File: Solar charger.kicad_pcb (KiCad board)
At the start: 2 copper layers, 70 x 32.5 mm, 12 parts, among them U1 MCP1700x-330xxTO

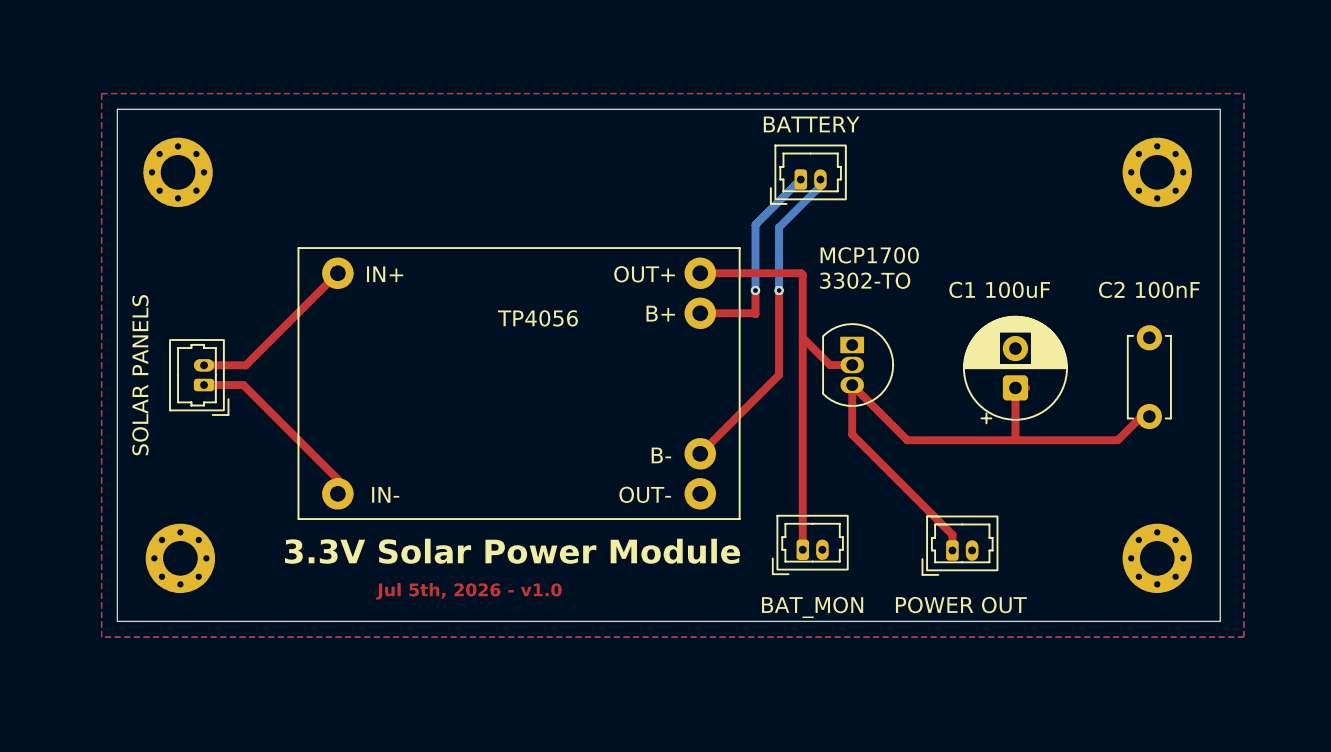
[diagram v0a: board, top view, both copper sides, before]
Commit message: Replace micro JSTs with terminal blocks (#3)
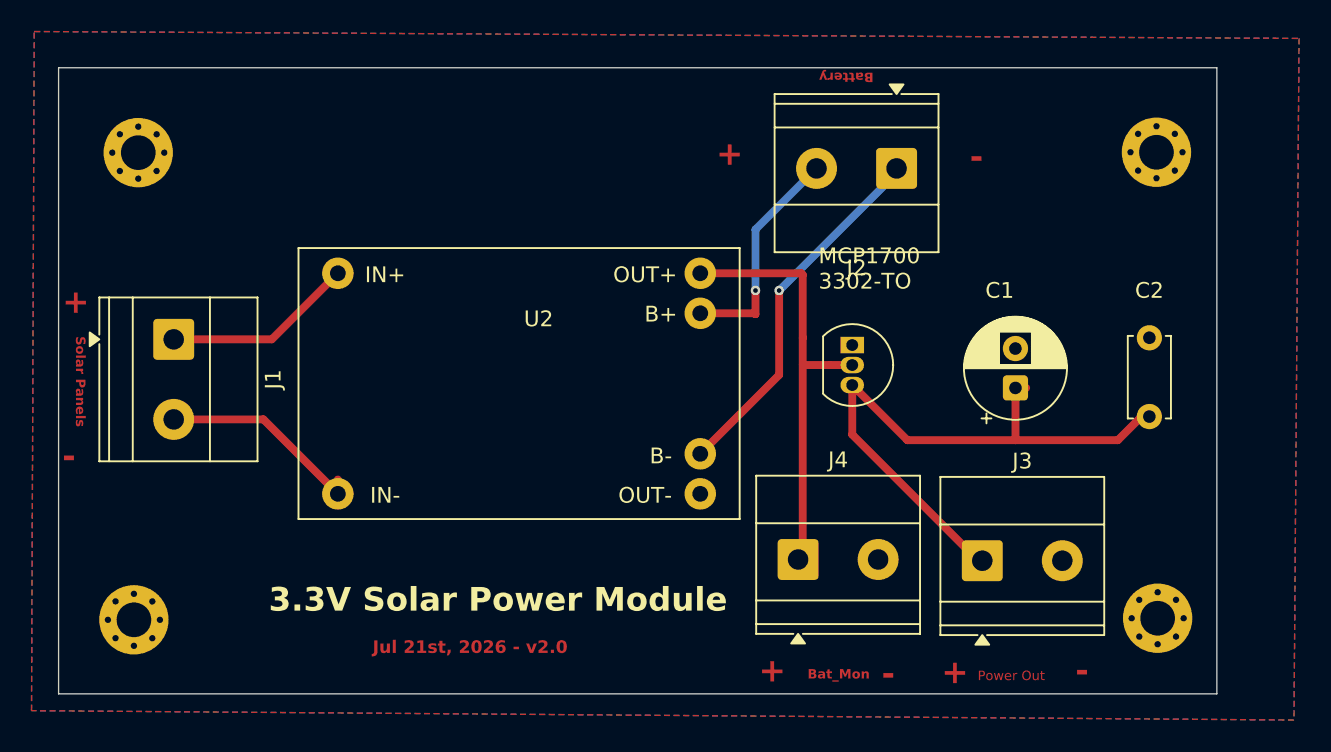
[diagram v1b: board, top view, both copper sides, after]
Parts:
- removed BATTERY: BATTERY, Connector_Molex:Molex_PicoBlade_53047-0210_1x02_P1.25mm_Vertical
- removed BAT_MON: BAT_MON, Connector_Molex:Molex_PicoBlade_53047-0210_1x02_P1.25mm_Vertical
- removed POWER OUT: POWER_OUT, Connector_Molex:Molex_PicoBlade_53047-0210_1x02_P1.25mm_Vertical
- removed SOLAR PANELS: SOLAR_IN, Connector_Molex:Molex_PicoBlade_53047-0210_1x02_P1.25mm_Vertical
- added J1: SOLAR_IN, TerminalBlock_Phoenix:TerminalBlock_Phoenix_MKDS-1,5-2-5.08_1x02_P5.08mm_Horizontal, F.Cu at (159.6, 86.6)
- added J2: BATTERY, TerminalBlock_Phoenix:TerminalBlock_Phoenix_MKDS-1,5-2-5.08_1x02_P5.08mm_Horizontal, F.Cu at (205.5, 75.8)
- added J3: POWER_OUT, TerminalBlock_Phoenix:TerminalBlock_Phoenix_MKDS-1,5-2-5.08_1x02_P5.08mm_Horizontal, F.Cu at (210.9, 100.7)
- added J4: BAT_MON, TerminalBlock_Phoenix:TerminalBlock_Phoenix_MKDS-1,5-2-5.08_1x02_P5.08mm_Horizontal, F.Cu at (199.2, 100.6)
- C1: renamed from C1 100uF
- C2: renamed from C2 100nF
- moved H2 4.89 mm to (157.1, 104.4)
- moved H3 3.80 mm to (222.0, 104.3)
- moved H1 2.82 mm to (157.3, 74.8)
- moved H4 1.28 mm to (221.9, 74.7)
- renumbered TP4056 to U2
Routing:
- net /BAT_GND: track 20.6 -> 23.3 mm
- net /3V3 OUT: track 38.1 -> 39.6 mm
- net /SOLAR_GND: track 11.9 -> 13.3 mm
- net /SOLAR_IN: track 10.9 -> 12.2 mm
- net /BAT_IN: track 13.3 -> 14.4 mm
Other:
- board size 70 x 32.5 mm -> 73.5 x 39.7 mm
- board text added: "+"
- board text added: "-"
- board text added: "Bat_Mon"
- board text added: "Battery"
- board text added: "Jul 21st, 2026 - v2.0"
- board text added: "Power Out"
- board text added: "Solar Panels"
- board text removed: "Jul 5th, 2026 - v1.0"
